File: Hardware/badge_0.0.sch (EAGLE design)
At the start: 43 parts, among them CON1 PH_2, IC1 CP2102, SW1 MK12C02, SW2 MK12C02, U4 MCP73832T-2DCI/OT

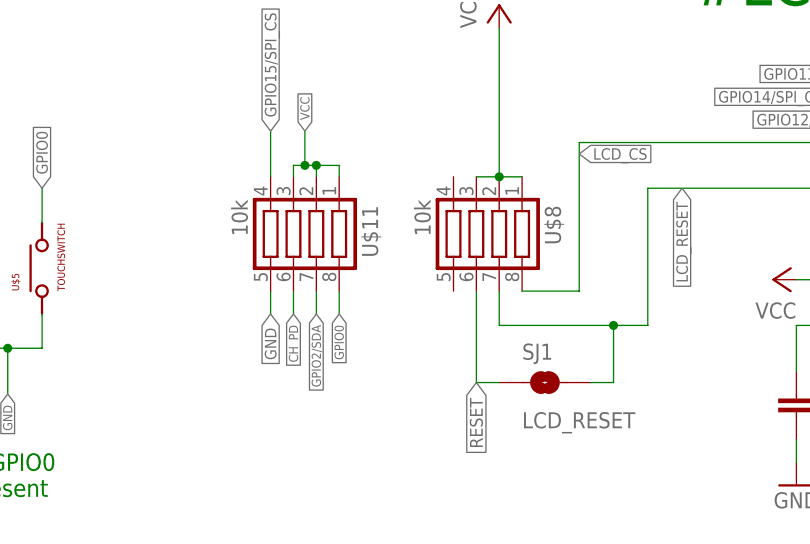
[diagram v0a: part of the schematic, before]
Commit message: Rerouted stuff. Added new power supply headers near LCD
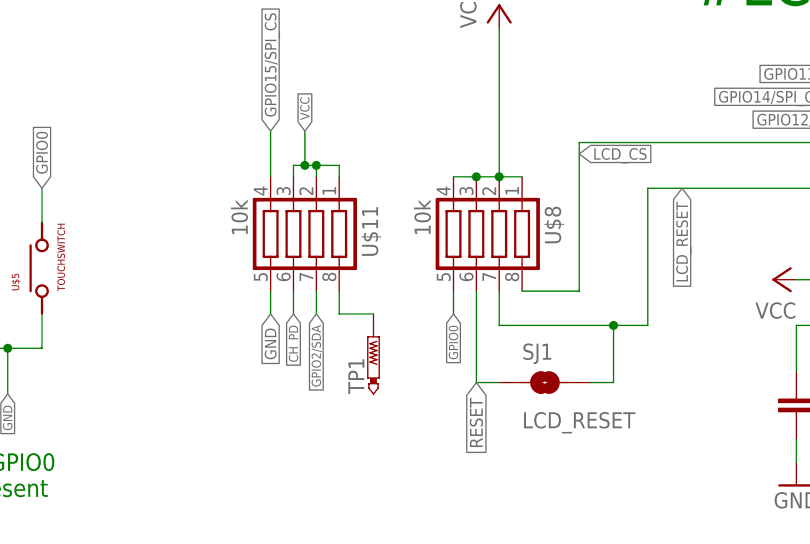
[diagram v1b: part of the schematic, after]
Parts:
- added TP1: PTR1B1,27, testpad:PTR1B1,27
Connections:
- new net N$3: TP1.TP, U$11.8
- net GPIO0: now also U$8.5; no longer U$11.8
- net VCC: now also U$8.4
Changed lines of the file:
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@@
 <part name="J3" library="SparkFun-Connectors" deviceset="M16" device="PTH"/>
 <part name="J4" library="SparkFun-Connectors" deviceset="M08" device=""/>
+<part name="TP1" library="testpad" deviceset="PTR1" device="B1,27"/>
 </parts>
 <sheets>
@@
 <instance part="J3" gate="G$1" x="199.39" y="149.86" rot="MR180"/>
 <instance part="J4" gate="G$1" x="344.17" y="165.1" rot="R180"/>
+<instance part="TP1" gate="G$1" x="124.46" y="46.99"/>
 </instances>
 <busses>
@@
 <pinref part="U$8" gate="G$1" pin="3"/>
 <wire x1="135.89" y1="64.77" x2="138.43" y2="64.77" width="0.1524" layer="91"/>
+<pinref part="U$8" gate="G$1" pin="4"/>
+<wire x1="135.89" y1="64.77" x2="133.35" y2="64.77" width="0.1524" layer="91"/>
+<junction x="135.89" y="64.77"/>
 </segment>
 <segment>
@@
 </segment>
 <segment>
-<label x="120.65" y="49.53" size="1.016" layer="95" rot="R270" xref="yes"/>
-<pinref part="U$11" gate="G$1" pin="8"/>
-<wire x1="120.65" y1="52.07" x2="120.65" y2="49.53" width="0.1524" layer="91"/>
+<label x="133.35" y="49.53" size="1.016" layer="95" rot="R270" xref="yes"/>
+<pinref part="U$8" gate="G$1" pin="5"/>
+<wire x1="133.35" y1="49.53" x2="133.35" y2="52.07" width="0.1524" layer="91"/>
 </segment>
 <segment>
@@
 </segment>
 </net>
+<net name="N$3" class="0">
+<segment>
+<pinref part="U$11" gate="G$1" pin="8"/>
+<wire x1="120.65" y1="52.07" x2="120.65" y2="49.53" width="0.1524" layer="91"/>
+<pinref part="TP1" gate="G$1" pin="TP"/>
+<wire x1="120.65" y1="49.53" x2="124.46" y2="49.53" width="0.1524" layer="91"/>
+</segment>
+</net>

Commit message: May not have saved for last commit
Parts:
- added J5, J6: (no value), SparkFun-Connectors:M04PTH
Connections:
- net GND: now also J5.3, J5.4, J6.3, J6.4
- net VCC: now also J5.1, J5.2, J6.1, J6.2
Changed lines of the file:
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@@
 <part name="J4" library="SparkFun-Connectors" deviceset="M08" device=""/>
 <part name="TP1" library="testpad" deviceset="PTR1" device="B1,27"/>
+<part name="J5" library="SparkFun-Connectors" deviceset="M04" device="PTH"/>
+<part name="J6" library="SparkFun-Connectors" deviceset="M04" device="PTH"/>
 </parts>
 <sheets>
@@
 <instance part="J4" gate="G$1" x="344.17" y="165.1" rot="R180"/>
 <instance part="TP1" gate="G$1" x="124.46" y="46.99"/>
+<instance part="J5" gate="G$1" x="345.44" y="222.25"/>
+<instance part="J6" gate="G$1" x="359.41" y="222.25"/>
 </instances>
 <busses>
@@
 <wire x1="334.01" y1="154.94" x2="339.09" y2="154.94" width="0.1524" layer="91"/>
 <label x="334.01" y="154.94" size="1.016" layer="95" rot="R180" xref="yes"/>
+</segment>
+<segment>
+<pinref part="J5" gate="G$1" pin="1"/>
+<pinref part="J5" gate="G$1" pin="2"/>
+<wire x1="350.52" y1="222.25" x2="350.52" y2="220.98" width="0.1524" layer="91"/>
+<pinref part="J6" gate="G$1" pin="1"/>
+<pinref part="J6" gate="G$1" pin="2"/>
+<wire x1="364.49" y1="222.25" x2="364.49" y2="220.98" width="0.1524" layer="91"/>
+<wire x1="364.49" y1="220.98" x2="364.49" y2="219.71" width="0.1524" layer="91"/>
+<junction x="364.49" y="220.98"/>
+<wire x1="364.49" y1="220.98" x2="368.3" y2="220.98" width="0.1524" layer="91"/>
+<wire x1="364.49" y1="220.98" x2="350.52" y2="220.98" width="0.1524" layer="91"/>
+<junction x="350.52" y="220.98"/>
+<wire x1="350.52" y1="220.98" x2="350.52" y2="219.71" width="0.1524" layer="91"/>
+<label x="368.3" y="220.98" size="1.27" layer="95" ratio="6" xref="yes"/>
 </segment>
 </net>
@@
 <label x="113.03" y="49.53" size="1.27" layer="95" ratio="6" rot="R270" xref="yes"/>
 </segment>
+<segment>
+<pinref part="J5" gate="G$1" pin="4"/>
+<pinref part="J5" gate="G$1" pin="3"/>
+<wire x1="350.52" y1="227.33" x2="350.52" y2="226.06" width="0.1524" layer="91"/>
+<wire x1="350.52" y1="226.06" x2="350.52" y2="224.79" width="0.1524" layer="91"/>
+<wire x1="350.52" y1="226.06" x2="364.49" y2="226.06" width="0.1524" layer="91"/>
+<junction x="350.52" y="226.06"/>
+<pinref part="J6" gate="G$1" pin="4"/>
+<wire x1="364.49" y1="226.06" x2="364.49" y2="227.33" width="0.1524" layer="91"/>
+<pinref part="J6" gate="G$1" pin="3"/>
+<wire x1="364.49" y1="224.79" x2="364.49" y2="226.06" width="0.1524" layer="91"/>
+<junction x="364.49" y="226.06"/>
+<wire x1="364.49" y1="226.06" x2="368.3" y2="226.06" width="0.1524" layer="91"/>
+<label x="368.3" y="226.06" size="1.27" layer="95" ratio="6" xref="yes"/>
+</segment>
 </net>

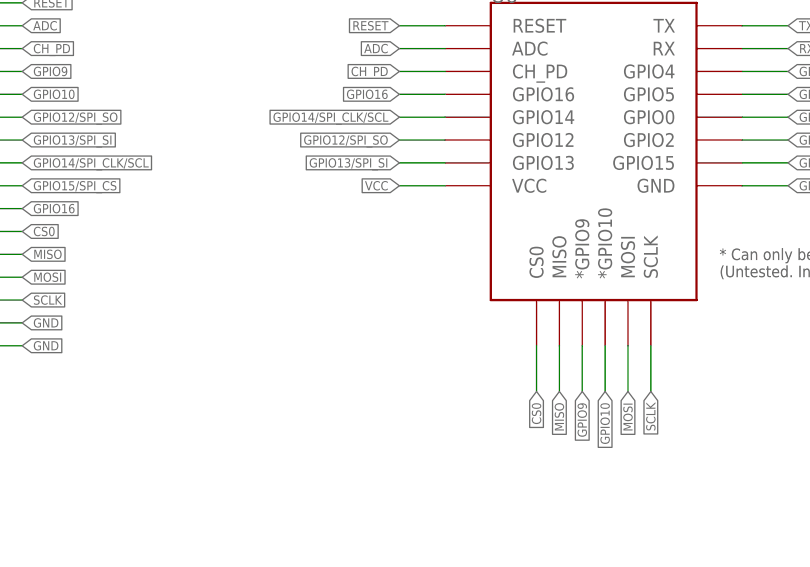
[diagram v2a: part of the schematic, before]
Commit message: added decoup cap; antenna gnd plane; minor edits;
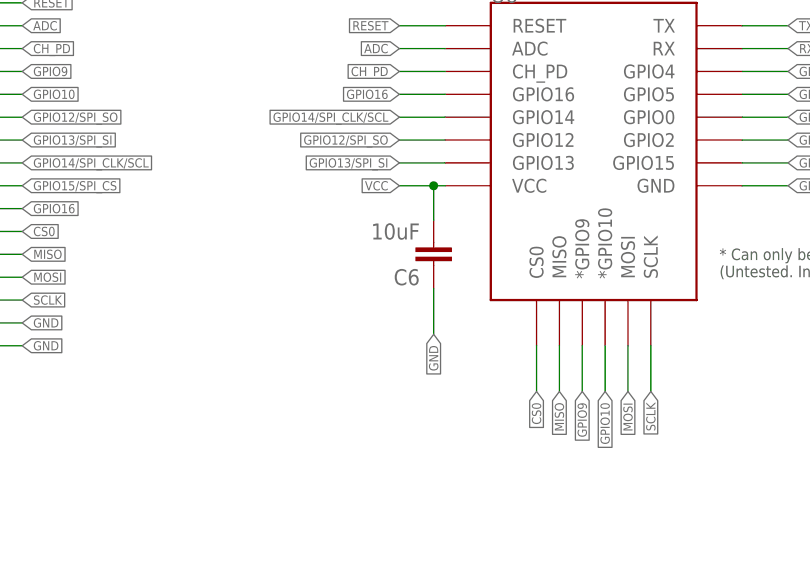
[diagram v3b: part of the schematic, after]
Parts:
- added C6: 10uF, resistor:C-EUC0603K
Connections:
- net GND: now also C6.1
- net VCC: now also C6.2
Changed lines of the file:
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@@
 <?xml version="1.0" encoding="utf-8"?>
 <!DOCTYPE eagle SYSTEM "eagle.dtd">
-<eagle version="7.1.0">
+<eagle version="7.5.0">
 <drawing>
 <settings>
@@
 <part name="J5" library="SparkFun-Connectors" deviceset="M04" device="PTH"/>
 <part name="J6" library="SparkFun-Connectors" deviceset="M04" device="PTH"/>
+<part name="C6" library="resistor" deviceset="C-EU" device="C0603K" value="10uF"/>
 </parts>
 <sheets>
@@
 <instance part="J5" gate="G$1" x="345.44" y="222.25"/>
 <instance part="J6" gate="G$1" x="359.41" y="222.25"/>
+<instance part="C6" gate="G$1" x="259.08" y="140.97" rot="R180"/>
 </instances>
 <busses>
@@
 <segment>
 <pinref part="U6" gate="G$1" pin="VCC"/>
-<wire x1="255.27" y1="149.86" x2="260.35" y2="149.86" width="0.1524" layer="91"/>
+<wire x1="255.27" y1="149.86" x2="259.08" y2="149.86" width="0.1524" layer="91"/>
 <label x="255.27" y="149.86" size="1.016" layer="95" rot="R180" xref="yes"/>
+<pinref part="C6" gate="G$1" pin="2"/>
+<wire x1="259.08" y1="149.86" x2="260.35" y2="149.86" width="0.1524" layer="91"/>
+<wire x1="259.08" y1="149.86" x2="259.08" y2="146.05" width="0.1524" layer="91"/>
+<junction x="259.08" y="149.86"/>
 </segment>
 <segment>
@@
 <label x="368.3" y="226.06" size="1.27" layer="95" ratio="6" xref="yes"/>
 </segment>
+<segment>
+<pinref part="C6" gate="G$1" pin="1"/>
+<wire x1="259.08" y1="138.43" x2="259.08" y2="133.35" width="0.1524" layer="91"/>
+<label x="259.08" y="133.35" size="1.016" layer="95" rot="R270" xref="yes"/>
+</segment>
 </net>
